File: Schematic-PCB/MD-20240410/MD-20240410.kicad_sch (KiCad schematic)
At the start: 0 parts

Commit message: メイン基板・MD基盤の更新
メイン基板 : ネオピクセルをPWM出力可能なピンに設定

MD基盤 : 電源回路の作成　DRV887x系の回路図参考・DRV8874製品ページ画像参考の2通りの回路を作成
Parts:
- added C1: 22n, symbol Device:C
- added C2: 220n, symbol Device:C
- added C3, C4: 4.7u, symbol Device:C
- added C5: 22nF, symbol Device:C
- added C6: 220nF, symbol Device:C
- added C7, C8: 0.1u, symbol Device:C
- added D2: 16.2V, symbol Device:D_Zener
- added Q2: PMOS, symbol Simulation_SPICE:PMOS
- added R1, R4: 2.49k, symbol Device:R
- added R2: 10K, symbol Device:R_Small
- added R5: 100k, symbol Device:R
- added U1, U3: ~, symbol @MyLibrary:DRV8874
- added U2: ~, symbol @MyLibrary:DRV887x
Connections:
- new net: D2.2 (A), Q2.2 (G), R5.1
- new net: C5.1, U1.13 (CPH)
- new net: C5.2, U1.14 (CPL)
- new net: R2.1, U1.5 (VREF)
- new net: C2.2, U2.12 (VCP)
- new net: C1.1, U2.13 (CPH)
- new net: C1.2, U2.14 (CPL)
- new net: R1.1, U1.6 (IPROPI)
- new net: C6.2, U1.12 (VCP)
- new net +5V: R2.2, U1.3 (SLEEP), U2.3 (SLEEP)
- new net 1-EN: U1.1 (EN/IN1), U2.1 (EN/IN1), U3.7 (EN/IN2)
- new net 1-IMODE: U1.7 (IMODE)
- new net 1-OUT1: U1.8 (OUT1), U2.8 (OUT1), U3.5 (OUT1)
- new net 1-OUT2: U1.10 (OUT2), U2.10 (OUT2), U3.6 (OUT2)
- new net 1-PH: U1.2 (EN/IN2), U2.2 (EN/IN2), U3.8 (PH/IN2)
- new net 1-PMODE: U1.16 (PMODE)
- new net 1-nFAULT: U1.4 (FAULT)
- new net GND: C3.2, C4.2, C7.2, C8.2, R1.2, R4.2, R5.2, U1.15 (GND), U1.17 (PAD), U1.9 (PGND), U2.15 (GND), U2.16 (PMODE), U3.2 (GND), U3.4 (GND), U3.9 (PMODE)
- new net VCC: U3.1 (VIN), U3.10 (SLEEP)
- new net VIN: Q2.1 (D)
- new net VM: C2.1, C3.1, C4.1, C6.1, C7.1, C8.1, D2.1 (K), Q2.3 (S), U1.11 (VM)
- no-connect marks 0 -> 12
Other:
- note added: "DRV8874の製品ページ画像を参考に作成"
- note added: "DRV887xの回路図を参考に作成"
- note added: "power"

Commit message: MD回路図の更新
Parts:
- removed C5: 22nF, symbol Device:C
- removed C6: 220nF, symbol Device:C
- removed R1: 2.49k, symbol Device:R
- removed R2: 10K, symbol Device:R_Small
- removed U1: ~, symbol @MyLibrary:DRV8874
- removed U2: ~, symbol @MyLibrary:DRV887x
- added C10, C12, C14: 220n, symbol Device:C
- added C11, C13, C9: 22n, symbol Device:C
- added R10, R14, R18, R6: NP, symbol Device:R
- added R11, R15, R19, R7: 20k, symbol Device:R
- added R12, R16, R8: 2.49k, symbol Device:R
- added R13, R17, R3, R9: 10k, symbol Device:R
- added U2, U4, U5: ~, symbol @MyLibrary:DRV8874
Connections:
- net 1-OUT2 is gone; now on an unnamed net: U3.6 (IPROPI)
- net GND: now also U3.15 (GND), U3.16 (PMODE), R10.2, R11.2, R12.2, R14.2, R15.2, R16.2, R18.2, R19.2, R6.2, R7.2, R8.2, U2.15 (GND), U2.16 (PMODE), U2.9 (PGND), U4.15 (GND), U4.16 (PMODE), U4.9 (PGND), U5.15 (GND), U5.16 (PMODE), U5.9 (PGND); no longer U3.2 (GND), U3.4 (GND)
- net VM: now also C2.2, U3.11 (VM), C10.2, C12.2, C14.2, U2.11 (VM), U4.11 (VM), U5.11 (VM); no longer C2.1
- net at C1.1: now also U3.14 (CPL)
- net at C1.2: now also U3.13 (CPH)
- net at U3.12 (VCP): now also C2.1
- net SLEEP-1: now reaches U3.3 (SLEEP)
- net SLEEP-1: now also R3.1
- net 1-EN renamed IMODE-1
- net IMODE-1: now also R7.1
- net 1-OUT1 renamed VREF-1
- net VREF-1: now also R3.2, R6.1
- net 1-PH renamed OUT-1
- net VCC renamed EN-1
- net EN-1: no longer U3.10 (SLEEP)
- new net: R16.1, U5.6 (IPROPI)
- new net: C10.1, U2.12 (VCP)
- new net: C9.2, U2.13 (CPH)
- new net: C9.1, U2.14 (CPL)
- new net: R8.1, U2.6 (IPROPI)
- new net: C12.1, U4.12 (VCP)
- new net: C14.1, U5.12 (VCP)
- new net: C11.1, U4.14 (CPL)
- new net: C11.2, U4.13 (CPH)
- new net: C13.2, U5.13 (CPH)
- new net: C13.1, U5.14 (CPL)
- new net: R12.1, U4.6 (IPROPI)
- new net EN-2: U2.1 (EN)
- new net EN-3: U4.1 (EN)
- new net EN-4: U5.1 (EN)
- new net IMODE-2: R11.1, U2.7 (IMODE)
- new net IMODE-3: R15.1, U4.7 (IMODE)
- new net IMODE-4: R19.1, U5.7 (IMODE)
- new net OUT1-2: U2.8 (OUT1)
- new net OUT1-3: U4.8 (OUT1)
- new net OUT1-4: U5.8 (OUT1)
- new net OUT2-1: U3.10 (OUT2)
- new net OUT2-2: U2.10 (OUT2)
- new net OUT2-3: U4.10 (OUT2)
- new net OUT2-4: U5.10 (OUT2)
- new net PH-1: U3.2 (PH)
- new net PH-2: U2.2 (PH)
- new net PH-3: U4.2 (PH)
- new net PH-4: U5.2 (PH)
- new net SLEEP-2: R9.1, U2.3 (SLEEP)
- new net SLEEP-3: R13.1, U4.3 (SLEEP)
- new net SLEEP-4: R17.1, U5.3 (SLEEP)
- new net VREF-2: R10.1, R9.2, U2.5 (VREF)
- new net VREF-3: R13.2, R14.1, U4.5 (VREF)
- new net VREF-4: R17.2, R18.1, U5.5 (VREF)
- no-connect marks 12 -> 4
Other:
- note added: "MD1"
- note added: "MD2"
- note added: "MD3"
- note added: "MD4"
- note removed: "DRV8874の製品ページ画像を参考に作成"
- note removed: "DRV887xの回路図を参考に作成"
- moved on the sheet: C2, C3, C4, C7, C8, D2, Q2, R4, R5

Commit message: メイン基板・MD基板の回路図を更新しました
10ピンコネクタの追加　電源電圧の修正
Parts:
- added C5: 50u, symbol Device:C
- added J1: Conn_01x02_Pin, symbol Connector:Conn_01x02_Pin
- added J2: Conn_01x10_Pin, symbol Connector:Conn_01x10_Pin
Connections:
- net EN-1: now also J2.1 (Pin_1)
- net EN-2: now also J2.3 (Pin_3)
- net EN-3: now also J2.5 (Pin_5)
- net EN-4: now also J2.7 (Pin_7)
- net GND: now also C5.2, J1.2 (Pin_2), J2.10 (Pin_10)
- net PH-1: now also J2.2 (Pin_2)
- net PH-2: now also J2.4 (Pin_4)
- net PH-3: now also J2.6 (Pin_6)
- net PH-4: now also J2.8 (Pin_8)
- net VM: now also C5.1
- net OUT-1 renamed OUT1-1
- net VIN renamed VCC
- net VCC: now also J1.1 (Pin_1)
- new net +3.3V: J2.9 (Pin_9)

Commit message: メイン基板・MD基板を修正しました
DR 2024.04.11 を参考に、メイン基板・MD基板を修正しました
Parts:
- added D1: LED, symbol Device:LED
- added J3, J4, J5, J6: Conn_01x02_Pin, symbol Connector:Conn_01x02_Pin
- added R1: 330, symbol Device:R
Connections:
- net +3.3V: now also U2.3 (SLEEP), U3.3 (SLEEP), U4.3 (SLEEP), U5.3 (SLEEP), R1.1
- net GND: now also D1.1 (K)
- net OUT1-1: now also J3.1 (Pin_1)
- net OUT1-2: now also J4.1 (Pin_1)
- net OUT1-3: now also J5.1 (Pin_1)
- net OUT1-4: now also J6.1 (Pin_1)
- net OUT2-1: now also J3.2 (Pin_2)
- net OUT2-2: now also J4.2 (Pin_2)
- net OUT2-3: now also J5.2 (Pin_2)
- net OUT2-4: now also J6.2 (Pin_2)
- net SLEEP-1: no longer U3.3 (SLEEP)
- net SLEEP-2: no longer U2.3 (SLEEP)
- net SLEEP-3: no longer U4.3 (SLEEP)
- net SLEEP-4: no longer U5.3 (SLEEP)
- new net: D1.2 (A), R1.2
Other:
- note added: "CONNECTOR"
- note added: "INPUT"
- note added: "LED"
- note added: "OUT"
- note added: "POWER"
- note removed: "power"
- moved on the sheet: C1, C10, C11, C12, C13, C14, C2, C3, C4, C5, C7, C8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

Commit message: MDのフットプリントを一部指定
フットプリントの確認をお願いします
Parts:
- removed J1: Conn_01x02_Pin, symbol Connector:Conn_01x02_Pin
- removed J2: Conn_01x10_Pin, symbol Connector:Conn_01x10_Pin
- added J1, J2: Conn_01x04_Pin, Connector_FFC-FPC:TE_84953-4_1x04-1MP_P1.0mm_Horizontal, symbol Connector:Conn_01x04_Pin
- added J7: Conn_01x03_Pin, Connector_JST:JST_XH_B3B-XH-A_1x03_P2.50mm_Vertical, symbol Connector:Conn_01x03_Pin
- C1, C10, C11, C12, C13, C14, C2, C3, C4, C5, C7, C8, C9: footprint (none) -> Capacitor_SMD:C_0603_1608Metric
- D1: footprint (none) -> LED_SMD:LED_0805_2012Metric
- J3, J4, J5, J6: footprint (none) -> Connector_JST:JST_XH_B2B-XH-A_1x02_P2.50mm_Vertical
- Q2: footprint (none) -> Package_TO_SOT_SMD:SOT-23
- R1, R10, R11, R12, R13, R14, R15, R16, R17, R18, R19, R3, R4, R5, R6, R7, R8, R9: footprint (none) -> Resistor_SMD:R_0603_1608Metric
- U2, U3, U4, U5: footprint (none) -> Package_SO:HTSSOP-16-1EP_4.4x5mm_P0.65mm_EP3.4x5mm_Mask2.46x2.31mm_ThermalVias
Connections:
- net +3.3V: now also J7.1 (Pin_1)
- net EN-1: now also J1.1 (Pin_1)
- net EN-2: now also J1.3 (Pin_3)
- net EN-3: now also J2.1 (Pin_1)
- net EN-4: now also J2.3 (Pin_3)
- net GND: now also J7.3 (Pin_3)
- net PH-1: now also J1.2 (Pin_2)
- net PH-2: now also J1.4 (Pin_4)
- net PH-3: now also J2.2 (Pin_2)
- net PH-4: now also J2.4 (Pin_4)
- net VCC: now also J7.2 (Pin_2)
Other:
- note added: "LINE LEFT"
- note added: "LINE RIGHT"
- note removed: "CONNECTOR"
- note removed: "INPUT"

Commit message: MD基板へ部品を仮で配置
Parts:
- removed J1, J2: Conn_01x04_Pin, Connector_FFC-FPC:TE_84953-4_1x04-1MP_P1.0mm_Horizontal, symbol Connector:Conn_01x04_Pin
- removed J7: Conn_01x03_Pin, Connector_JST:JST_XH_B3B-XH-A_1x03_P2.50mm_Vertical, symbol Connector:Conn_01x03_Pin
- added J1, J2: Conn_01x05_Pin, Connector_FFC-FPC:TE_84953-5_1x05-1MP_P1.0mm_Horizontal, symbol Connector:Conn_01x05_Pin
- added J7: Conn_01x02_Pin, Connector_JST:JST_VH_B2P-VH_1x02_P3.96mm_Vertical, symbol Connector:Conn_01x02_Pin
- D2: footprint (none) -> Diode_SMD:D_SOD-323
- J3, J4, J5, J6: footprint Connector_JST:JST_XH_B2B-XH-A_1x02_P2.50mm_Vertical -> Connector_JST:JST_VH_B2P-VH_1x02_P3.96mm_Vertical
- Q2: footprint Package_TO_SOT_SMD:SOT-23 -> Package_TO_SOT_SMD:TO-252-2
- renumbered U3 to U1, U4 to U3, U5 to U4
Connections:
- net +3.3V: now also J1.5 (Pin_5)
- net EN-1: now also J1.1 (Pin_1)
- net EN-2: now also J1.3 (Pin_3)
- net EN-3: now also J2.1 (Pin_1)
- net EN-4: now also J2.3 (Pin_3)
- net GND: now also J2.5 (Pin_5), J7.2 (Pin_2)
- net PH-1: now also J1.2 (Pin_2)
- net PH-2: now also J1.4 (Pin_4)
- net PH-3: now also J2.2 (Pin_2)
- net PH-4: now also J2.4 (Pin_4)
- net VCC: now also J7.1 (Pin_1)

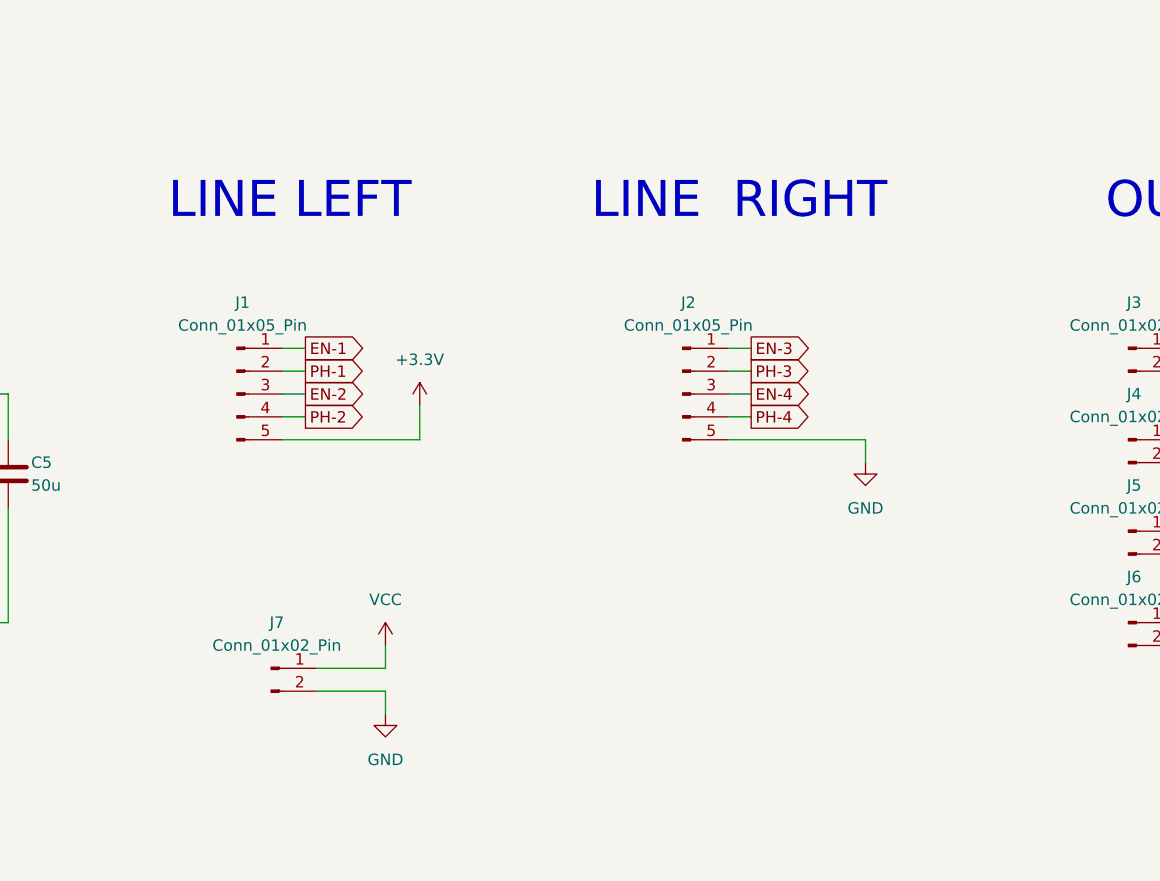
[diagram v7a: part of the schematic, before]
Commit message: MD・ラインセンサの回路図を更新
メイン→ラインセンサ→MD と配線していたのを、
メイン→MD→ラインセンサ と経由するように変更した。

ラインセンサの回路図へ、コンパレータを使用するパターンの回路を追加で作成した。
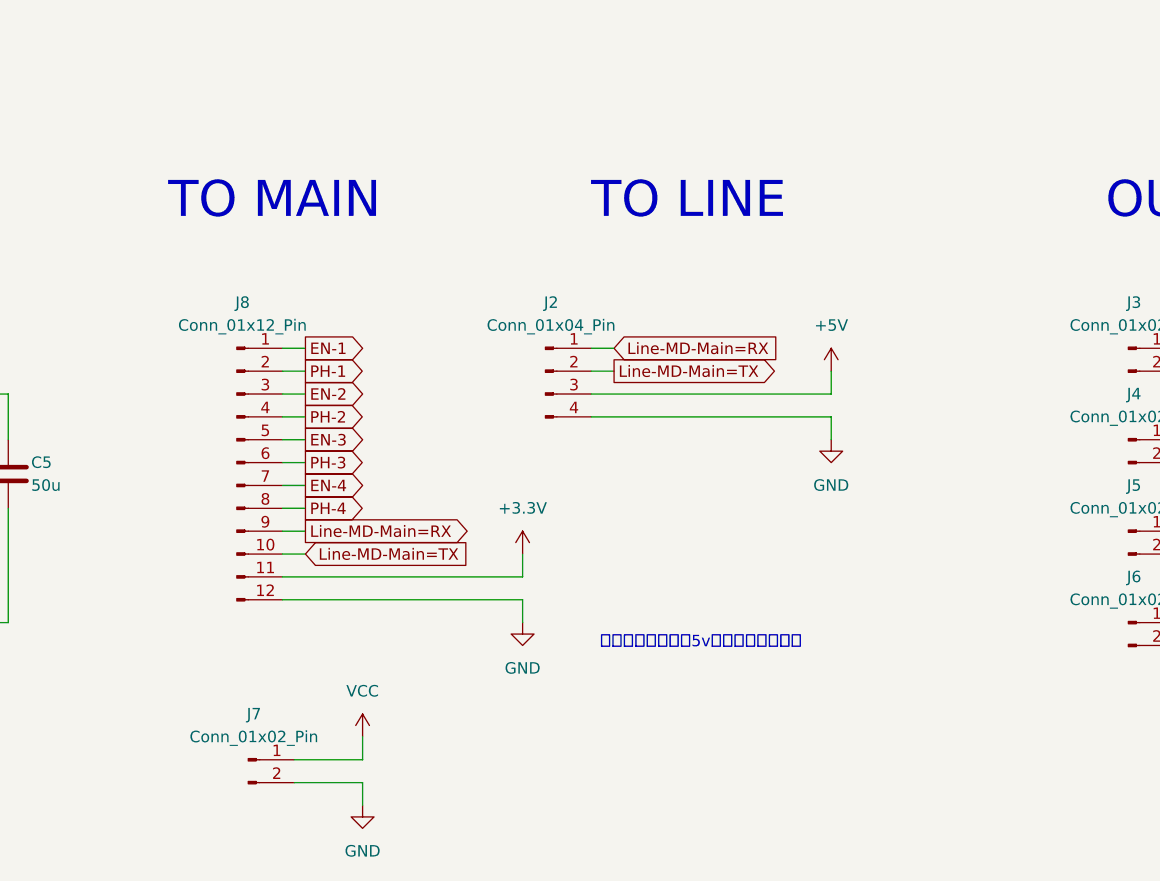
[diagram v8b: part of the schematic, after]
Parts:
- removed J1, J2: Conn_01x05_Pin, Connector_FFC-FPC:TE_84953-5_1x05-1MP_P1.0mm_Horizontal, symbol Connector:Conn_01x05_Pin
- added J2: Conn_01x04_Pin, symbol Connector:Conn_01x04_Pin
- added J8: Conn_01x12_Pin, symbol Connector:Conn_01x12_Pin
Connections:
- net +3.3V: now also J8.11 (Pin_11)
- net EN-1: now also J8.1 (Pin_1)
- net EN-2: now also J8.3 (Pin_3)
- net EN-3: now also J8.5 (Pin_5)
- net EN-4: now also J8.7 (Pin_7)
- net GND: now also J2.4 (Pin_4), J8.12 (Pin_12)
- net PH-1: now also J8.2 (Pin_2)
- net PH-2: now also J8.4 (Pin_4)
- net PH-3: now also J8.6 (Pin_6)
- net PH-4: now also J8.8 (Pin_8)
- new net +5V: J2.3 (Pin_3)
- new net Line-MD-Main=RX: J2.1 (Pin_1), J8.9 (Pin_9)
- new net Line-MD-Main=TX: J2.2 (Pin_2), J8.10 (Pin_10)
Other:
- note added: "TO LINE"
- note added: "TO MAIN"
- note added: "ラインセンサへの5v電源をどうするか"
- note removed: "LINE LEFT"
- note removed: "LINE RIGHT"
- moved on the sheet: J7
